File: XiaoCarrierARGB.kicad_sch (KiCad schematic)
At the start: 24 parts, among them J1 V_{IN}^{10-24V}, J2 Conn_01x06, J3 Conn_01x08, J4 Conn_01x08, J5 Conn_01x01, J6 Conn_01x01, U1 XIAO-ESP32-C6-DIP, U2 TPP362083-T6TR, U3 TLV75733PDBV, U4 74LVC1T45W6-7, U5 74LVC1T45W6-7, U6 74LVC1T45W6-7

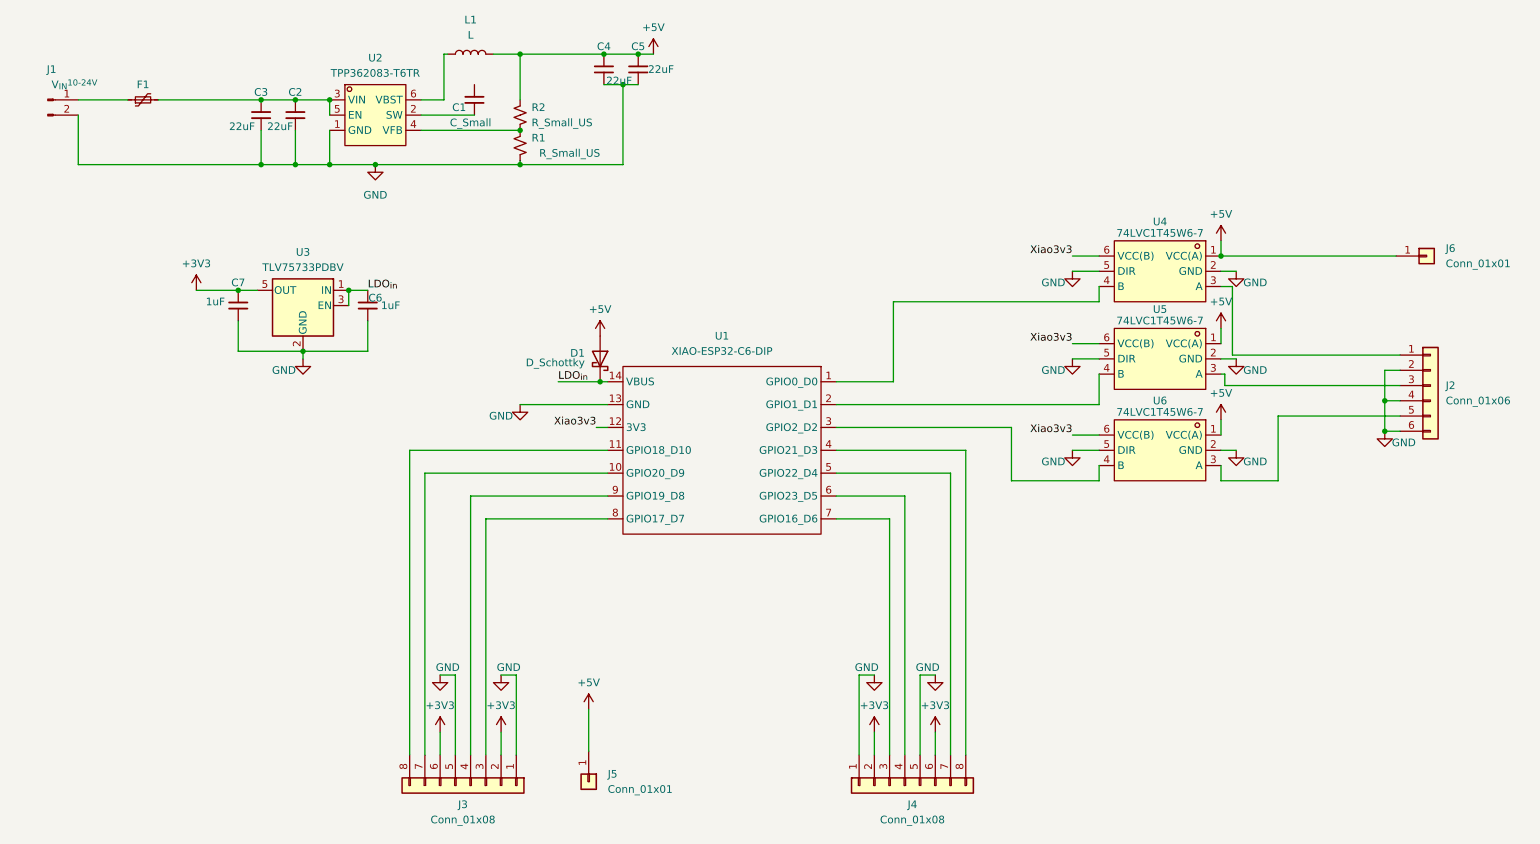
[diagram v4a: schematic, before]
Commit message: Mostly Finalized Schematic added footprint assignments and most BOM entries
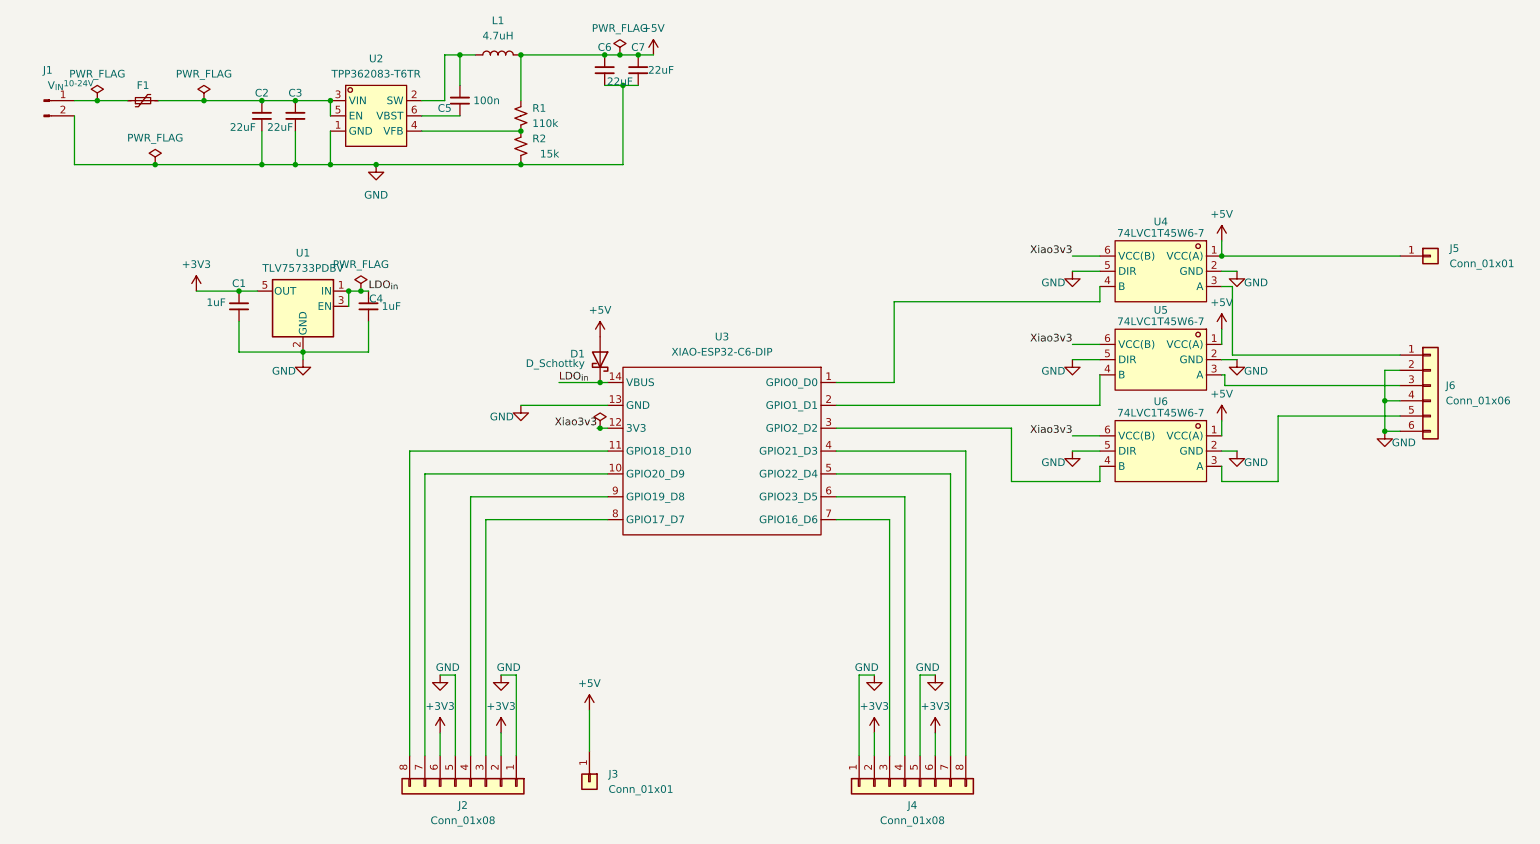
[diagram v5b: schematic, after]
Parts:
- C5: renamed from C1; value C_Small -> 100n
- D1: footprint Package_SON:WSON-8-1EP_6x5mm_P1.27mm_EP3.4x4mm -> Diode_SMD:D_SMA; DigiKey Part (none) -> 3757-SBA520AFC_R1_00001; LCSC Part (none) -> C7355752; MPN (none) -> SBA520AFC_R1_00001
- F1: DigiKey Part (none) -> 13-SMD1812B110TF/33; LCSC Part (none) -> C269134
- J1: footprint LED_THT:LED_D5.0mm_IRGrey -> Connector_PinHeader_2.54mm:PinHeader_1x02_P2.54mm_Vertical
- J2: renamed from J3; footprint Connector_RJ:RJ45_Abracon_ARJP11A-MA_Horizontal -> Connector_PinHeader_2.54mm:PinHeader_1x08_P2.54mm_Vertical
- J3: renamed from J5; footprint Connector_RJ:RJ45_Abracon_ARJP11A-MA_Horizontal -> Connector_PinHeader_2.54mm:PinHeader_1x01_P2.54mm_Vertical
- J4: footprint Connector_RJ:RJ45_Abracon_ARJP11A-MA_Horizontal -> Connector_PinHeader_2.54mm:PinHeader_1x08_P2.54mm_Vertical
- J5: renamed from J6; footprint Connector_RJ:RJ45_Abracon_ARJP11A-MA_Horizontal -> Connector_PinHeader_2.54mm:PinHeader_1x01_P2.54mm_Vertical
- J6: renamed from J2; footprint Connector_RJ:RJ45_Abracon_ARJP11A-MA_Horizontal -> Connector_PinHeader_2.54mm:PinHeader_1x06_P2.54mm_Vertical
- L1: value L -> 4.7uH; footprint (none) -> Inductor_SMD:L_Chilisin_BWVS00606045; DigiKey Part (none) -> 541-IFSC2020DEER4R7M01CT-ND; LCSC Part (none) -> C47327077; MPN (none) -> IFSC2020DEER4R7M01
- R1: renamed from R2; value R_Small_US -> 110k
- R2: renamed from R1; value R_Small_US -> 15k
- U2: DigiKey Part (none) -> 5503-TPP362081-T6TR; Digikey Part 5503-TPP362083-T6TR -> (none); LCSC Part C38493766 -> C29073195; MPN TPP362083-T6TR -> TPP362081-T6TR
- U3: renamed from U1; footprint Seeed_Studio_XIAO_Series:XIAO-ESP32-C6-DIP -> Seeed Xiao:XIAO-ESP32-C6-DIP
- renumbered C7 to C1, C3 to C2, C2 to C3, C6 to C4, C4 to C6, C5 to C7, U3 to U1
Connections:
- net at L1.1: now also C5.2, U2.2 (SW); no longer U2.6 (VBST)
- net at C5.1: now also U2.6 (VBST); no longer U2.2 (SW)
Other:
- moved on the sheet: C5, J1, J5, L1

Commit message: Started rough Layout considering dropping board size to 1.5in x2.5in 4 layers might be excessive
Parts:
- R1, R2: footprint Resistor_THT:R_Array_SIP4 -> Resistor_SMD:R_0805_2012Metric
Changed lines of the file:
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@@
 			)
 		)
-		(property "Footprint" "Resistor_THT:R_Array_SIP4"
+		(property "Footprint" "Resistor_SMD:R_0805_2012Metric"
 			(at 94.742 47.752 0)
 			(hide yes)
@@
 			)
 		)
-		(property "Footprint" "Resistor_THT:R_Array_SIP4"
+		(property "Footprint" "Resistor_SMD:R_0805_2012Metric"
 			(at 94.742 42.672 0)
 			(hide yes)

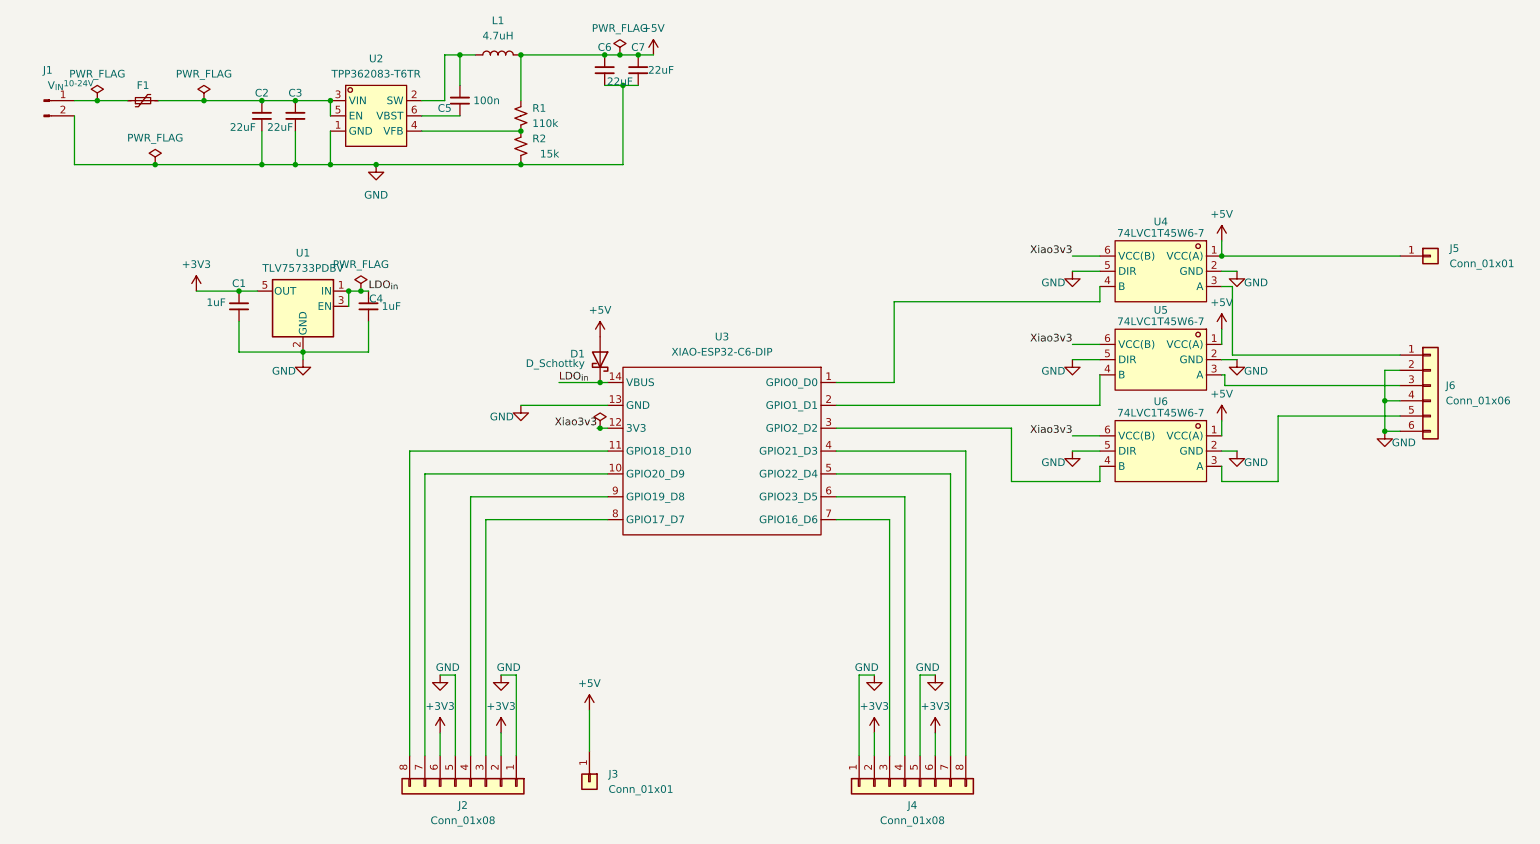
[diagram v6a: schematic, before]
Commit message: realigned schem grid added netclass assignment and net names
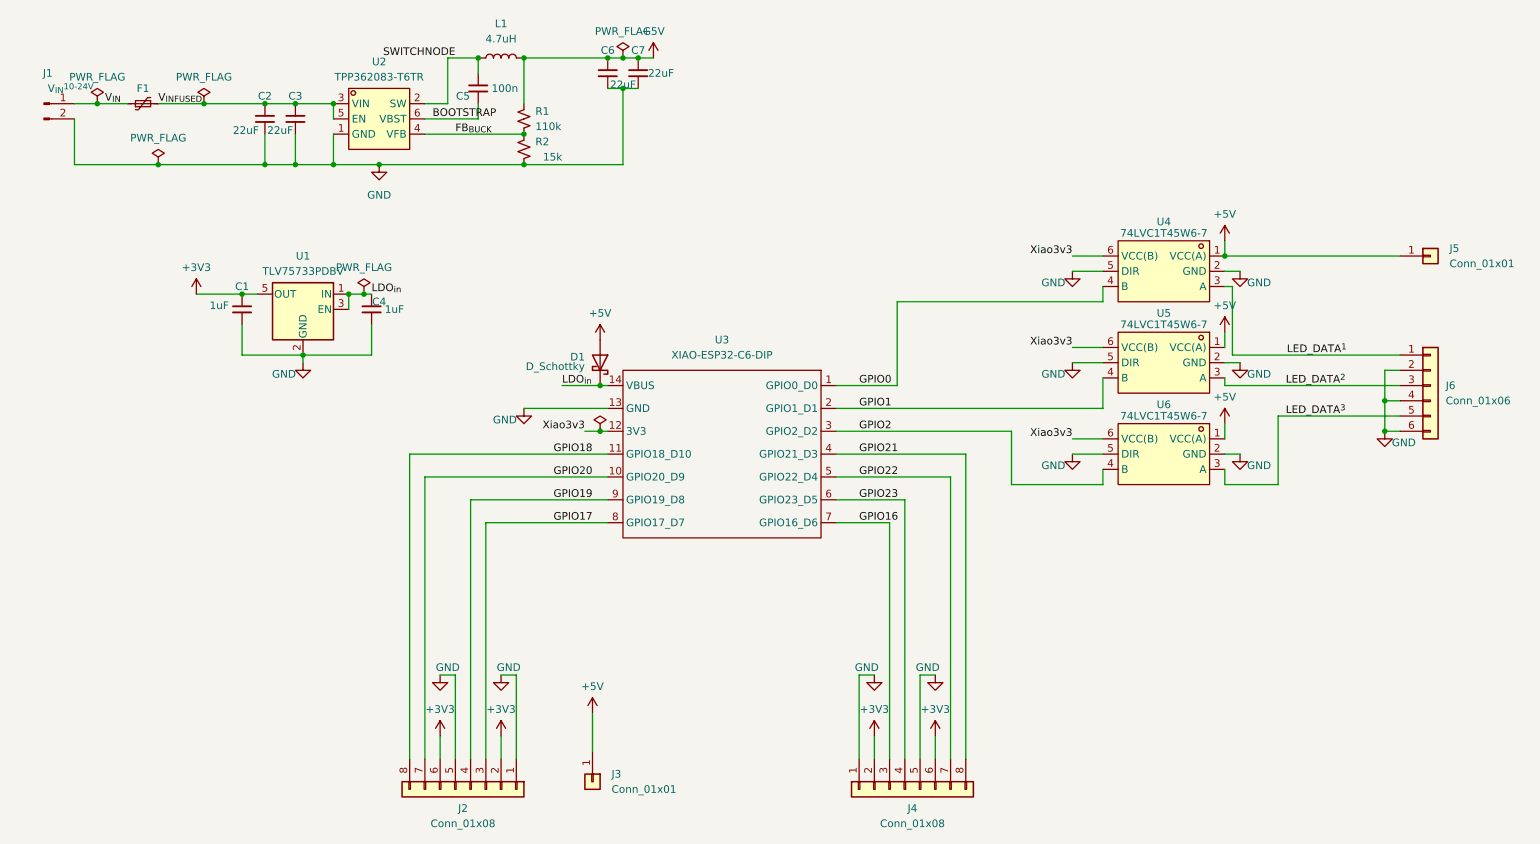
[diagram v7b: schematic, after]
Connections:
- net LED_DATA^{1}: now reaches J6.1 (Pin_1), U4.3 (A)
- net GPIO0: now reaches U3.1 (GPIO0_D0), U4.4 (B)
- net GPIO20: now reaches J2.7 (Pin_7), U3.10 (GPIO20_D9)
- net GPIO18: now reaches J2.8 (Pin_8), U3.11 (GPIO18_D10)
- net GPIO1: now reaches U3.2 (GPIO1_D1), U5.4 (B)
- net GPIO2: now reaches U3.3 (GPIO2_D2), U6.4 (B)
- net GPIO21: now reaches J4.8 (Pin_8), U3.4 (GPIO21_D3)
- net GPIO22: now reaches J4.7 (Pin_7), U3.5 (GPIO22_D4)
- net GPIO23: now reaches J4.4 (Pin_4), U3.6 (GPIO23_D5)
- net GPIO16: now reaches J4.3 (Pin_3), U3.7 (GPIO16_D6)
- net GPIO17: now reaches J2.3 (Pin_3), U3.8 (GPIO17_D7)
- net GPIO19: now reaches J2.4 (Pin_4), U3.9 (GPIO19_D8)
- net SWITCHNODE: now reaches C5.2, L1.1, U2.2 (SW)
- net LED_DATA^{2}: now reaches J6.3 (Pin_3), U5.3 (A)
- net FB_{BUCK}: now reaches R1.2, R2.1, U2.4 (VFB)
- net V_{IN}: now reaches F1.1, J1.1 (Pin_1)
- net V_{IN}_{FUSED}: now reaches C2.1, C3.1, F1.2, U2.3 (VIN), U2.5 (EN)
- net LED_DATA^{3}: now reaches J6.5 (Pin_5), U6.3 (A)
- net BOOTSTRAP: now reaches C5.1, U2.6 (VBST)
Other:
- moved on the sheet: C1, C2, C3, C4, C5, C6, C7, D1, F1, J1, J2, J3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

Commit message: Did mostly all layout need to sanity check and review
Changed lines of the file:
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@@
 	(wire
 		(pts
-			(xy 213.36 82.55) (xy 241.3 82.55)
+			(xy 214.63 82.55) (xy 241.3 82.55)
 		)
 		(stroke
@@
 	(wire
 		(pts
-			(xy 212.09 68.58) (xy 214.63 68.58)
+			(xy 212.09 68.58) (xy 217.17 68.58)
 		)
 		(stroke
@@
 	(wire
 		(pts
-			(xy 212.09 71.12) (xy 213.36 71.12)
+			(xy 212.09 71.12) (xy 214.63 71.12)
 		)
 		(stroke
@@
 	(wire
 		(pts
-			(xy 213.36 71.12) (xy 213.36 82.55)
+			(xy 214.63 71.12) (xy 214.63 82.55)
 		)
 		(stroke
@@
 	(symbol
 		(lib_id "power:GND")
-		(at 214.63 68.58 0)
+		(at 217.17 68.58 0)
 		(unit 1)
 		(body_style 1)
@@
 		(dnp no)
 		(property "Reference" "#PWR022"
-			(at 214.63 74.93 0)
+			(at 217.17 74.93 0)
 			(hide yes)
 			(show_name no)
@@
 		)
 		(property "Value" "GND"
-			(at 217.805 70.485 0)
+			(at 220.345 70.485 0)
 			(show_name no)
 			(do_not_autoplace no)
@@
 		)
 		(property "Footprint" ""
-			(at 214.63 68.58 0)
+			(at 217.17 68.58 0)
 			(hide yes)
 			(show_name no)
@@
 		)
 		(property "Datasheet" ""
-			(at 214.63 68.58 0)
+			(at 217.17 68.58 0)
 			(hide yes)
 			(show_name no)
@@
 		)
 		(property "Description" "Power symbol creates a global label with name \"GND\" , ground"
-			(at 214.63 68.58 0)
+			(at 217.17 68.58 0)
 			(hide yes)
 			(show_name no)
